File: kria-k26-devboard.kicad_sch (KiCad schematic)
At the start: 6 parts

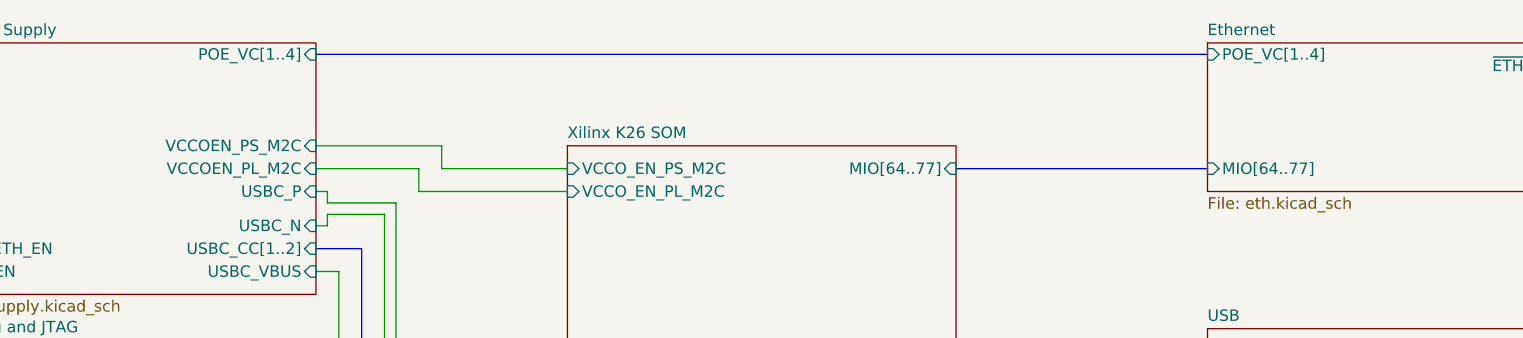
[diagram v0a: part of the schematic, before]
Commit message: removed PoE from schematic
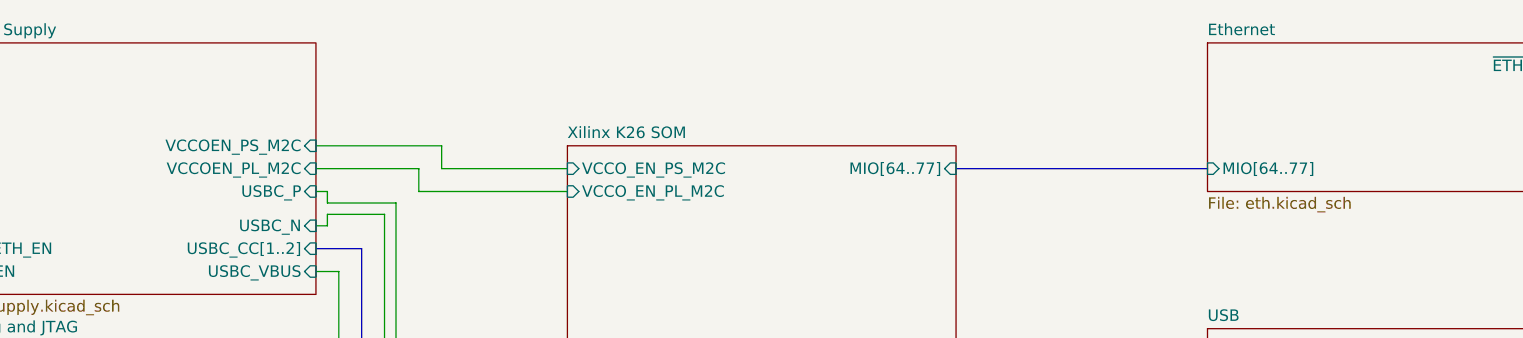
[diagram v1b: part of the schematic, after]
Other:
- sheet Ethernet ports: added none; removed POE_VC[1..4]
- sheet Power Supply ports: added none; removed POE_VC[1..4]
